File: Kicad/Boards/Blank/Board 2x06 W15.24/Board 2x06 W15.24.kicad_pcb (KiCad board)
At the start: 2 copper layers, 18.8 x 17.9 mm, 1 part, among them J1 Board 2x06 W15.24mm

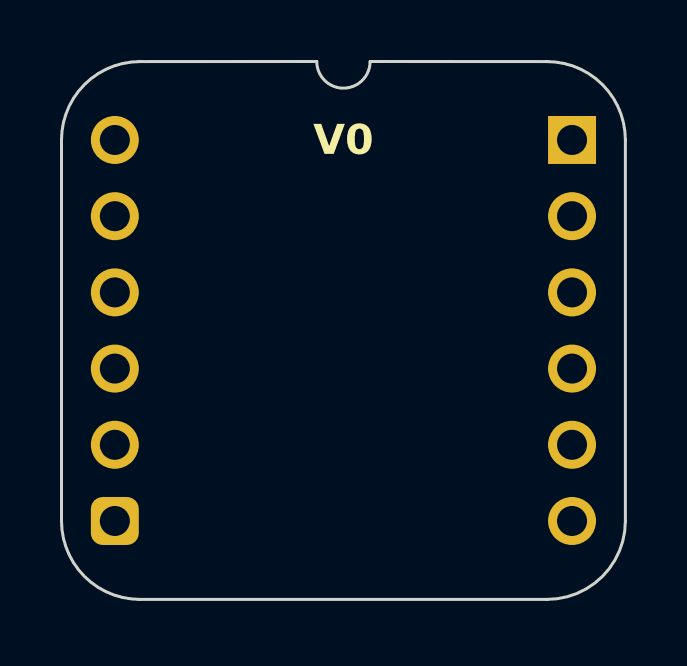
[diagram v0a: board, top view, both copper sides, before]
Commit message: Added some blank board projects.
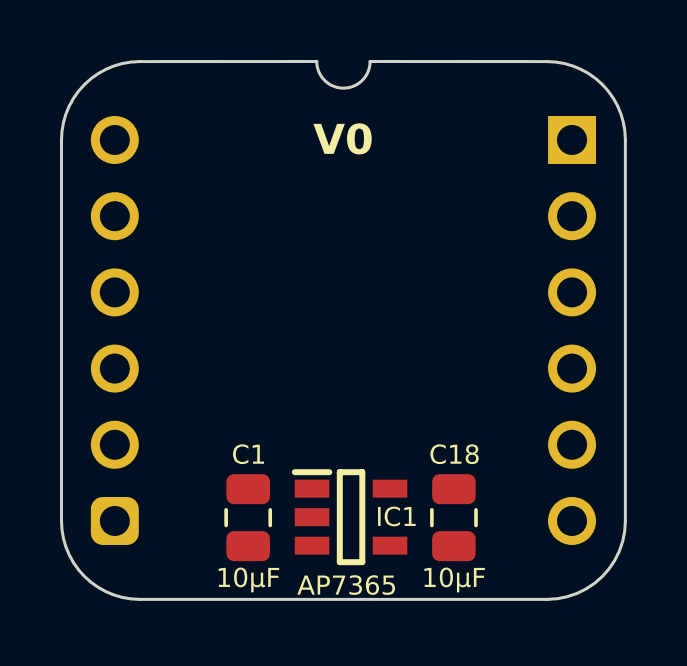
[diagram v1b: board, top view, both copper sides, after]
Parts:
- added C1: 10µF, SamacSys_Parts:C_0805, F.Cu at (4.45, 12.6)
- added C18: 10µF, SamacSys_Parts:C_0805, F.Cu at (11.3, 12.6)
- added IC1: AP7365-33WG-7, SamacSys_Parts:SOT95P285X130-5N, F.Cu at (7.87, 12.6)
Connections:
- J1 pad 12: unconnected-(J1-Pad12) -> GND
- J1 pad 6: unconnected-(J1-Pad6) -> 5V

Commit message: Added silkscreen and power components to some blank boards.
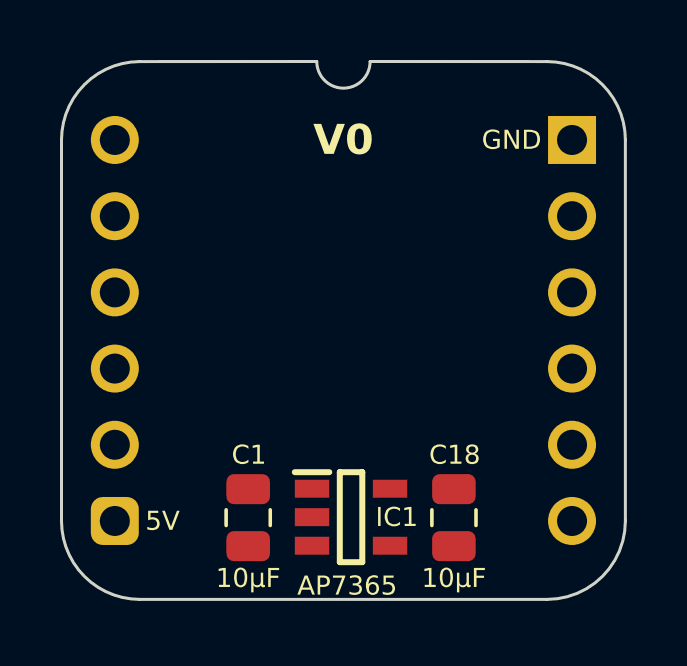
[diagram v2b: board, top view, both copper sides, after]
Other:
- board text added: "5V"
- board text added: "GND"
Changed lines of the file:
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@@
 	(title_block
 		(title "Board 2x06 W15.24mm")
-		(date "2025-09-29")
+		(date "2026-03-04")
 		(rev "V0")
 	)
@@
 		)
 	)
+	(gr_text "GND"
+		(at 14.224 0 0)
+		(layer "F.SilkS")
+		(effects
+			(font
+				(size 0.635 0.635)
+				(thickness 0.15)
+			)
+			(justify right)
+		)
+	)
+	(gr_text "5V"
+		(at 1.016 12.7 0)
+		(layer "F.SilkS")
+		(effects
+			(font
+				(size 0.635 0.635)
+				(thickness 0.15)
+			)
+			(justify left)
+		)
+	)
